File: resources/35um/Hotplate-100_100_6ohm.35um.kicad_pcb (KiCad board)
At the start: 2 copper layers, 100 x 100 mm, 7 parts, among them J1 Hotplate_Power_Connection, J2 Hotplate_Power_Connection

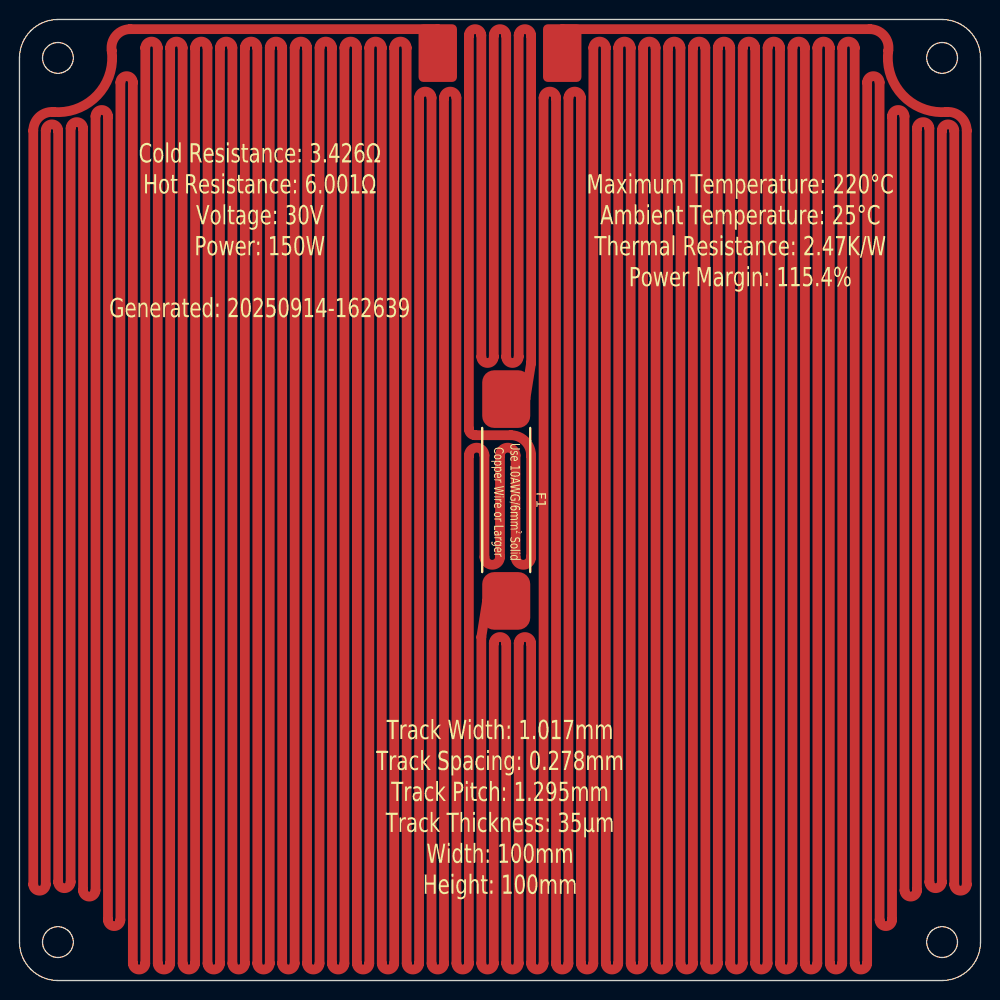
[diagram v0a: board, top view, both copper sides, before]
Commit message: Replaced obsolete 25mm thermal fuse footprint with new 35mm thermal fuse footprint.
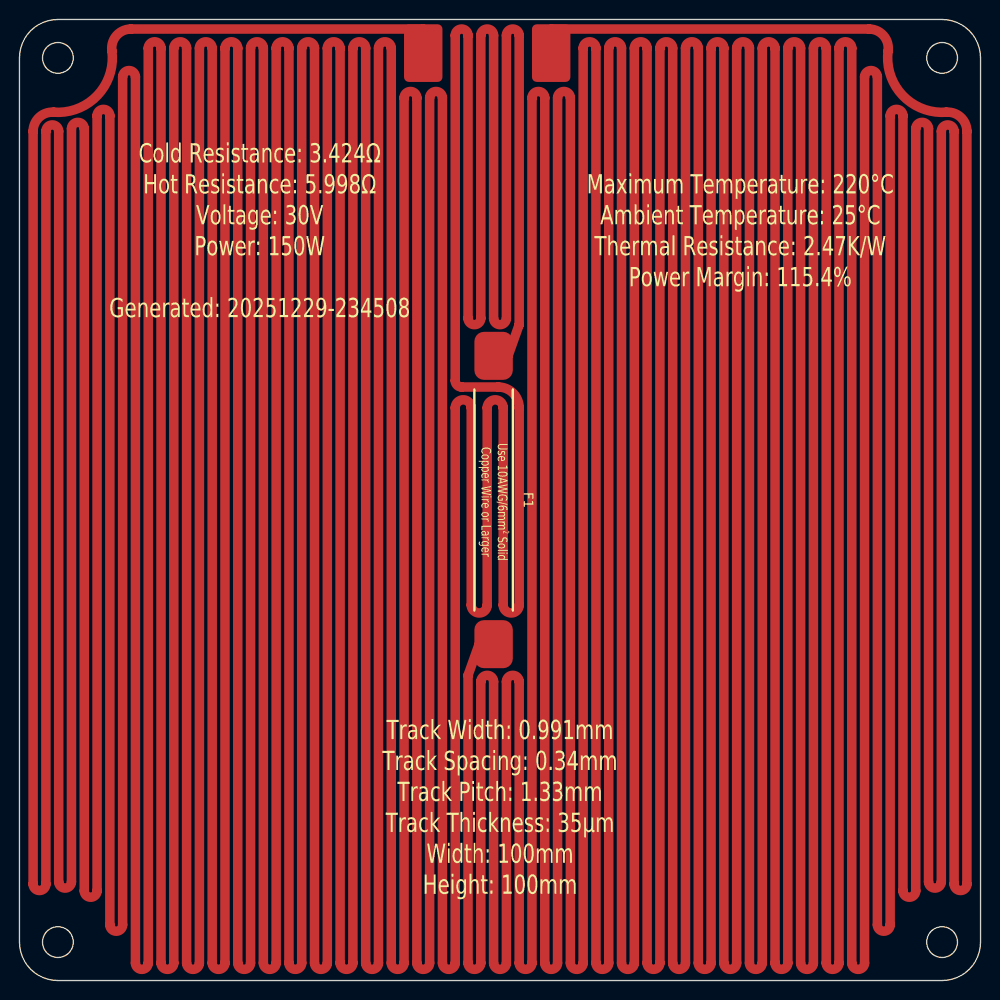
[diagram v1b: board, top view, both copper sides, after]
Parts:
- F1: footprint blg:Thermal Fuse, Front, 25mm -> blg:Thermal Fuse, SN100C, Front, 35mm
- moved J1 1.51 mm to (97.0, 58.5)
- moved F1 1.31 mm to (104.3, 105.0)
- moved J2 1.15 mm to (110.3, 58.5)
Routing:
- net Net-(J1-Pin_1): track 3642.2 -> 3467.9 mm
- net Net-(J2-Pin_1): track 3486.5 -> 3468.7 mm
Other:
- board text added: "Cold Resistance: 3.424Ω Hot Resistance: 5.998Ω Voltage: 30V Power: 150W Generated: 20251229-234508"
- board text added: "Track Width: 0.991mm Track Spacing: 0.34mm Track Pitch: 1.33mm Track Thickness: 35µm Width: 100mm Height: 100mm"
- board text removed: "Cold Resistance: 3.426Ω Hot Resistance: 6.001Ω Voltage: 30V Power: 150W Generated: 20250914-162639"
- board text removed: "Track Width: 1.017mm Track Spacing: 0.278mm Track Pitch: 1.295mm Track Thickness: 35µm Width: 100mm Height: 100mm"
